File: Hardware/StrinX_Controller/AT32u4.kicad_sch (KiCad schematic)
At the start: 19 parts, among them J1 HWB, SW1 RST, U1 ATmega32U4-A, Y1 16MHz

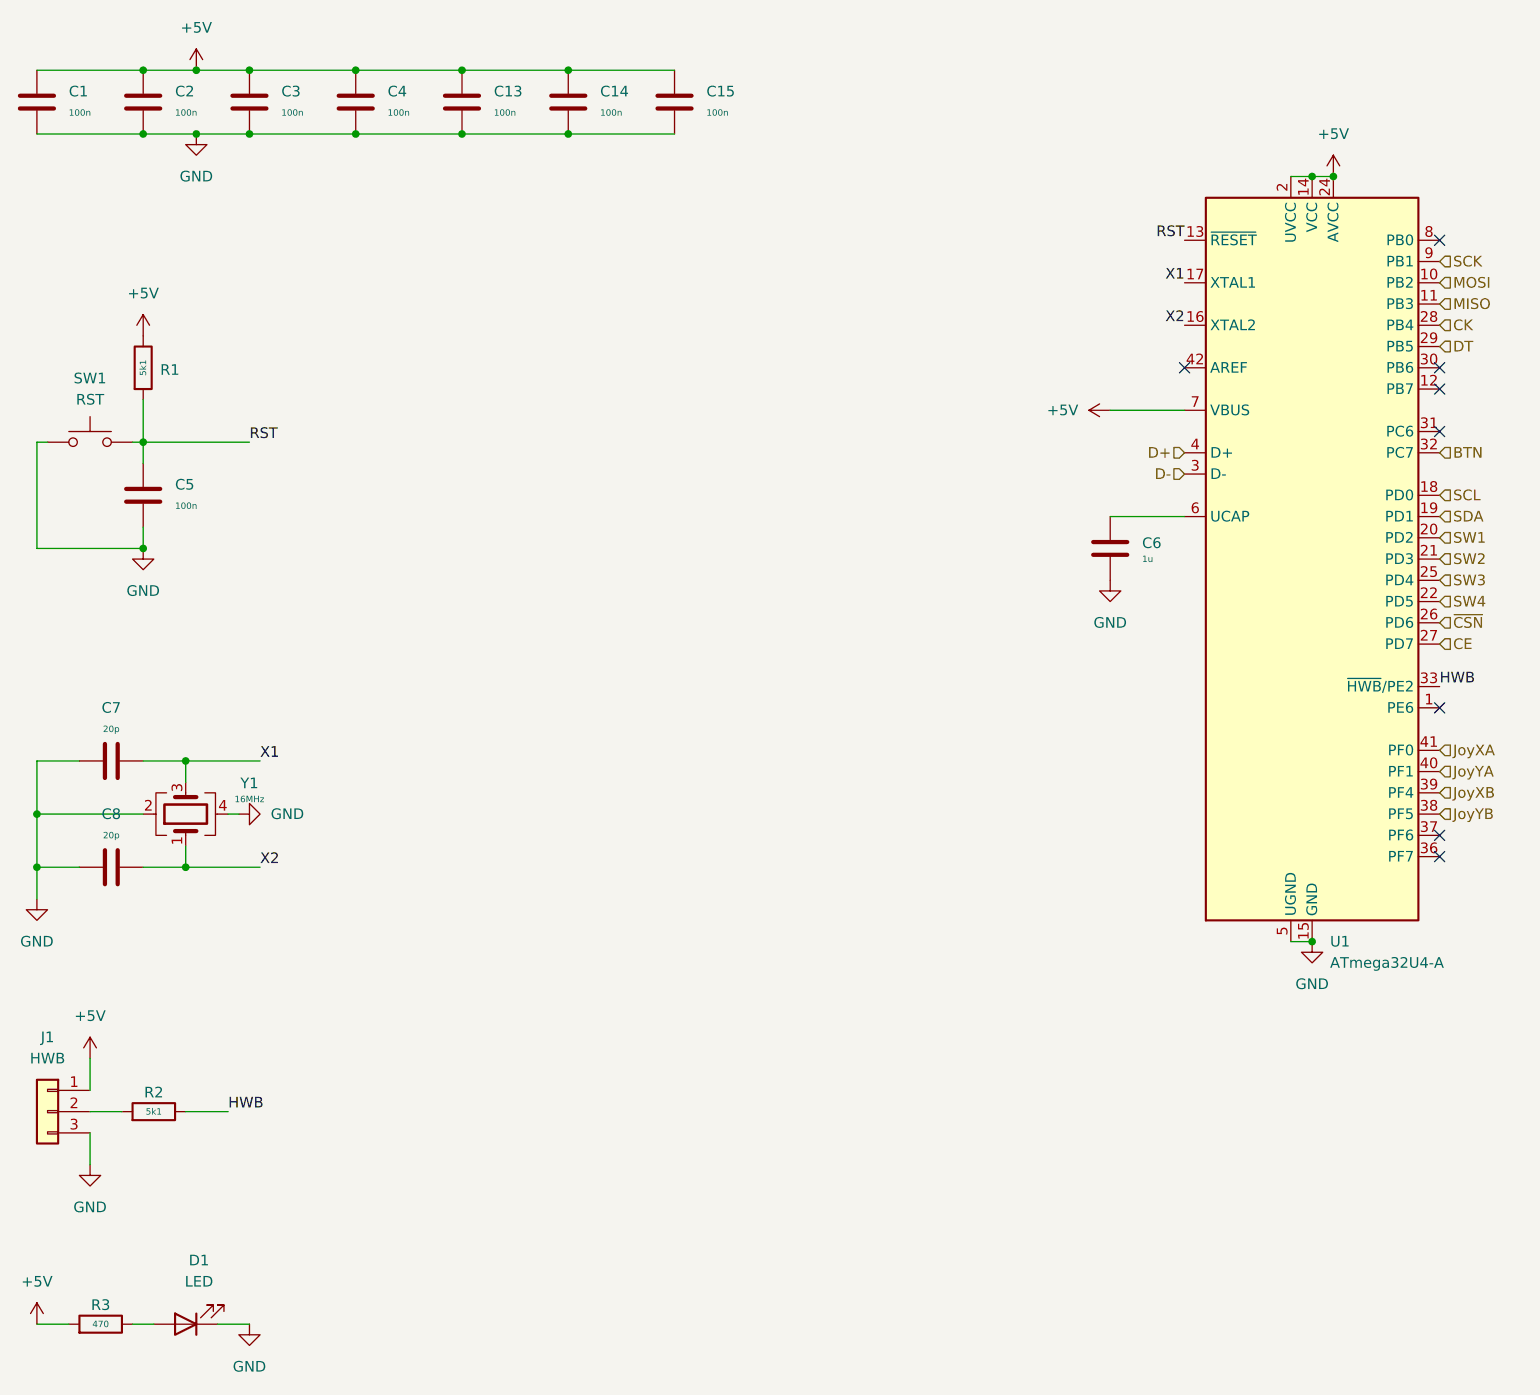
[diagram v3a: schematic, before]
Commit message: Update some device connection and Complete PCB
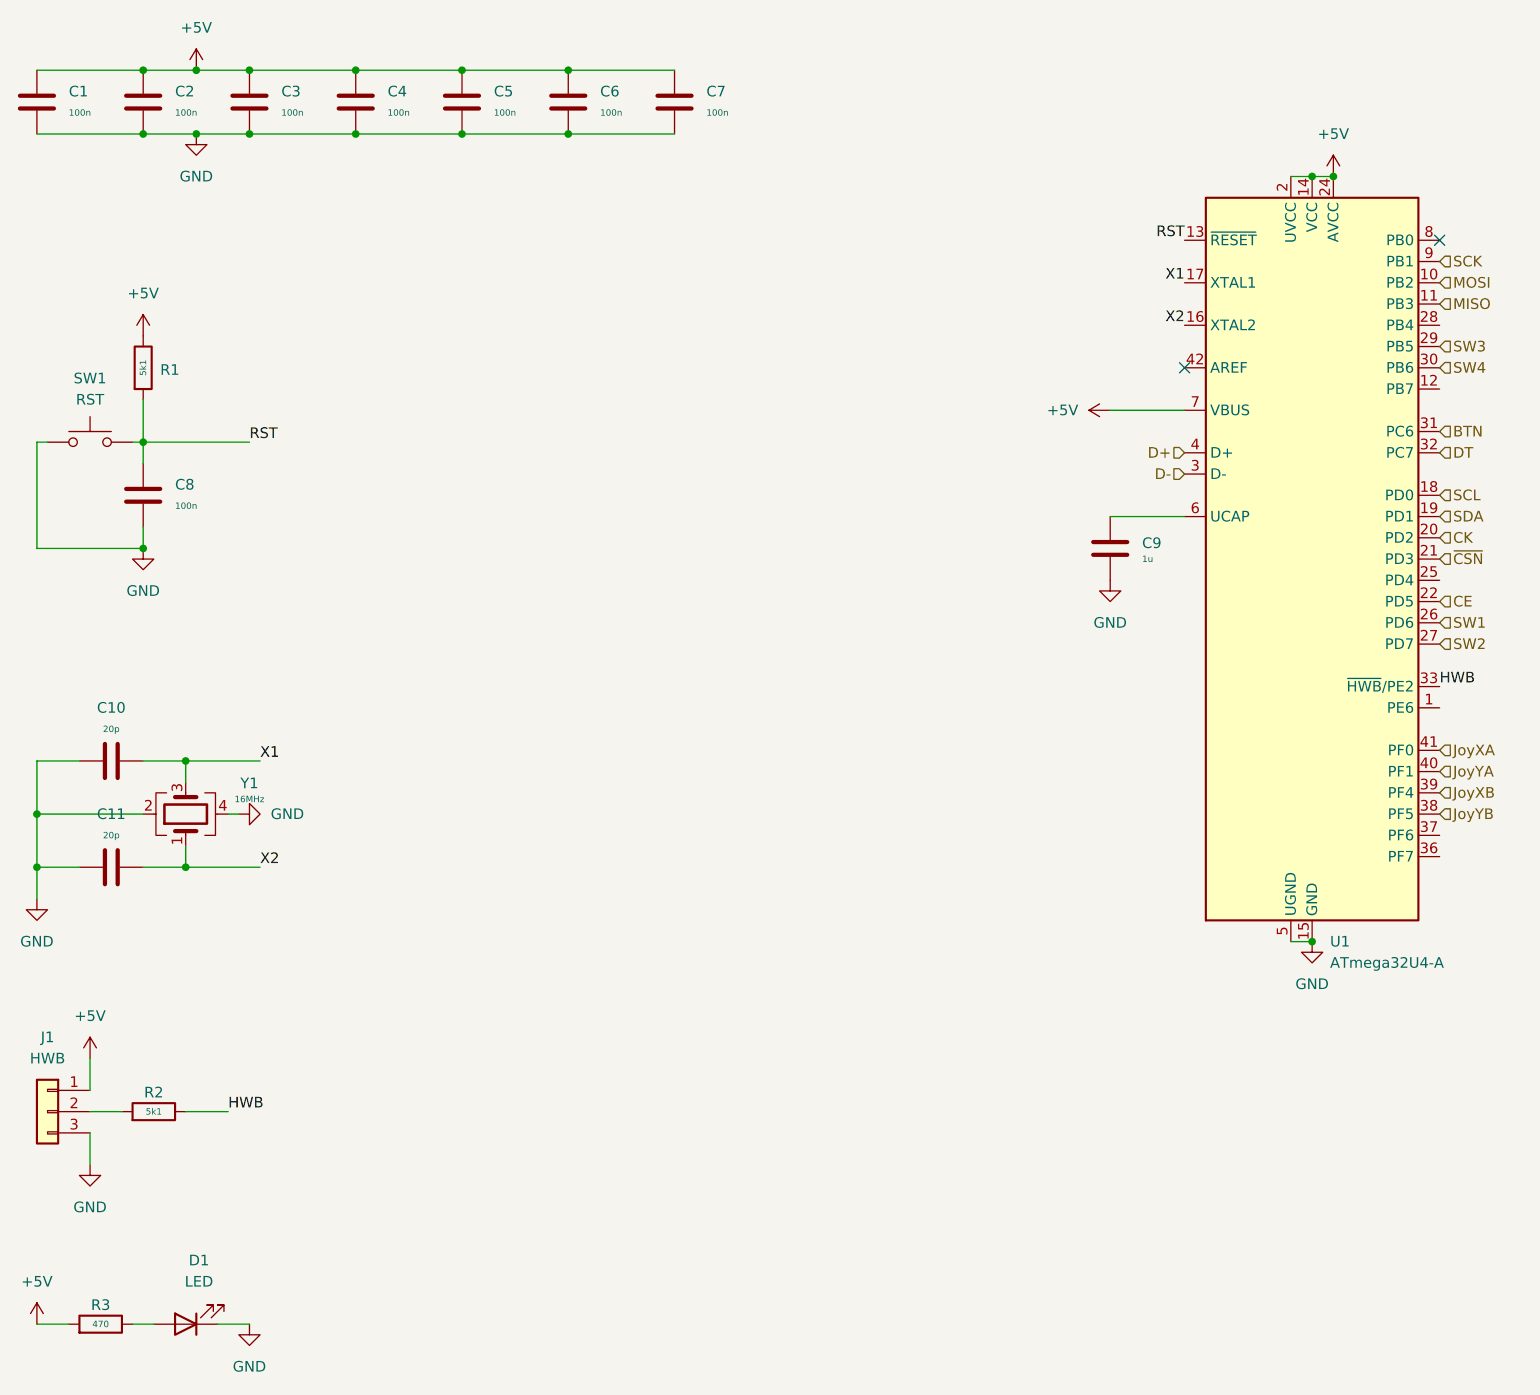
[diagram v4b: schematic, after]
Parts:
- renumbered C7 to C10, C8 to C11, C13 to C5, C14 to C6, C15 to C7, C5 to C8, C6 to C9
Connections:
- net BTN: now also U1.31 (PC6); no longer U1.32 (PC7)
- net CE: now also U1.22 (PD5); no longer U1.27 (PD7)
- net CK: now also U1.20 (PD2); no longer U1.28 (PB4)
- net DT: now also U1.32 (PC7); no longer U1.29 (PB5)
- net SW1: now also U1.26 (PD6); no longer U1.20 (PD2)
- net SW2: now also U1.27 (PD7); no longer U1.21 (PD3)
- net SW3: now also U1.29 (PB5); no longer U1.25 (PD4)
- net SW4: now also U1.30 (PB6); no longer U1.22 (PD5)
- net ~{CSN}: now also U1.21 (PD3); no longer U1.26 (PD6)
- no-connect marks 8 -> 2
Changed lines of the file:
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@@
-	)
-	(no_connect
-		(at 205.74 60.96)
-	)
-	(no_connect
-		(at 205.74 68.58)
-	)
-	(no_connect
-		(at 205.74 101.6)
 	)
 	(no_connect
@@
 	(no_connect
 		(at 205.74 45.72)
-	)
-	(no_connect
-		(at 205.74 119.38)
-	)
-	(no_connect
-		(at 205.74 116.84)
-	)
-	(no_connect
-		(at 205.74 63.5)
 	)
 	(wire
@@
 	(hierarchical_label "CE"
 		(shape input)
-		(at 205.74 93.98 0)
+		(at 205.74 88.9 0)
 		(effects
 			(font
@@
 	(hierarchical_label "CK"
 		(shape input)
-		(at 205.74 55.88 0)
+		(at 205.74 81.28 0)
 		(effects
 			(font
@@
 	(hierarchical_label "SW2"
 		(shape input)
-		(at 205.74 83.82 0)
+		(at 205.74 93.98 0)
 		(effects
 			(font
@@
 	(hierarchical_label "SW3"
 		(shape input)
-		(at 205.74 86.36 0)
+		(at 205.74 58.42 0)
 		(effects
 			(font
@@
 	(hierarchical_label "DT"
 		(shape input)
-		(at 205.74 58.42 0)
+		(at 205.74 71.12 0)
 		(effects
 			(font
@@
 	)
 	(hierarchical_label "~{CSN}"
+		(shape input)
+		(at 205.74 83.82 0)
+		(effects
+			(font
+				(size 1.27 1.27)
+			)
+			(justify left)
+		)
+	)
+	(hierarchical_label "SW4"
+		(shape input)
+		(at 205.74 60.96 0)
+		(effects
+			(font
+				(size 1.27 1.27)
+			)
+			(justify left)
+		)
+	)
+	(hierarchical_label "BTN"
+		(shape input)
+		(at 205.74 68.58 0)
+		(effects
+			(font
+				(size 1.27 1.27)
+			)
+			(justify left)
+		)
+	)
+	(hierarchical_label "SW1"
 		(shape input)
 		(at 205.74 91.44 0)
@@
 		)
 	)
-	(hierarchical_label "SW4"
-		(shape input)
-		(at 205.74 88.9 0)
-		(effects
-			(font
-				(size 1.27 1.27)
-			)
-			(justify left)
-		)
-	)
-	(hierarchical_label "BTN"
-		(shape input)
-		(at 205.74 71.12 0)
-		(effects
-			(font
-				(size 1.27 1.27)
-			)
-			(justify left)
-		)
-	)
-	(hierarchical_label "SW1"
-		(shape input)
-		(at 205.74 81.28 0)
-		(effects
-			(font
-				(size 1.27 1.27)
-			)
-			(justify left)
-		)
-	)
 	(symbol
 		(lib_id "Device:C")
@@
 		(dnp no)
 		(fields_autoplaced yes)
-		(property "Reference" "C7"
+		(property "Reference" "C10"
 			(at 46.99 101.6 90)
 			(effects
@@
 			(project "StrinX_Controller"
 				(path "/60efaa1b-44bb-4814-90d0-8b9990f45080/108dcd71-5b76-4a3d-a22d-e690a9401ff3"
-					(reference "C7")
+					(reference "C10")
 					(unit 1)
 				)
@@
 		(dnp no)
 		(fields_autoplaced yes)
-		(property "Reference" "C5"
+		(property "Reference" "C8"
 			(at 54.61 74.9299 0)
 			(effects
@@
 				)
 				(path "/60efaa1b-44bb-4814-90d0-8b9990f45080/108dcd71-5b76-4a3d-a22d-e690a9401ff3"
-					(reference "C5")
+					(reference "C8")
 					(unit 1)
 				)
@@
 		(dnp no)
 		(fields_autoplaced yes)
-		(property "Reference" "C8"
+		(property "Reference" "C11"
 			(at 46.99 114.3 90)
 			(effects
@@
 			(project "StrinX_Controller"
 				(path "/60efaa1b-44bb-4814-90d0-8b9990f45080/108dcd71-5b76-4a3d-a22d-e690a9401ff3"
-					(reference "C8")
+					(reference "C11")
 					(unit 1)
 				)
@@
 		(dnp no)
 		(fields_autoplaced yes)
-		(property "Reference" "C6"
+		(property "Reference" "C9"
 			(at 170.18 81.9149 0)
 			(effects
@@
 			(project "StrinX_Controller"
 				(path "/60efaa1b-44bb-4814-90d0-8b9990f45080/108dcd71-5b76-4a3d-a22d-e690a9401ff3"
-					(reference "C6")
+					(reference "C9")
 					(unit 1)
 				)
@@
 		(dnp no)
 		(fields_autoplaced yes)
-		(property "Reference" "C14"
+		(property "Reference" "C6"
 			(at 105.41 27.9399 0)
 			(effects
@@
 			(project "StrinX_Controller"
 				(path "/60efaa1b-44bb-4814-90d0-8b9990f45080/108dcd71-5b76-4a3d-a22d-e690a9401ff3"
-					(reference "C14")
+					(reference "C6")
 					(unit 1)
 				)
@@
 		(dnp no)
 		(fields_autoplaced yes)
-		(property "Reference" "C15"
+		(property "Reference" "C7"
 			(at 118.11 27.9399 0)
 			(effects
@@
 			(project "StrinX_Controller"
 				(path "/60efaa1b-44bb-4814-90d0-8b9990f45080/108dcd71-5b76-4a3d-a22d-e690a9401ff3"
-					(reference "C15")
+					(reference "C7")
 					(unit 1)
 				)
@@
 		(dnp no)
 		(fields_autoplaced yes)
-		(property "Reference" "C13"
+		(property "Reference" "C5"
 			(at 92.71 27.9399 0)
 			(effects
@@
 			(project "StrinX_Controller"
 				(path "/60efaa1b-44bb-4814-90d0-8b9990f45080/108dcd71-5b76-4a3d-a22d-e690a9401ff3"
-					(reference "C13")
-					(unit 1)
-				)
+					(reference "C5")
+					(unit 1)
+				)
